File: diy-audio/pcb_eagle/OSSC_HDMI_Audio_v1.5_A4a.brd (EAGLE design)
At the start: 29.9 x 16.9 mm, 29 parts, among them U1 PCM1808, U2 74LVC1G34, U3 MK2507SLF

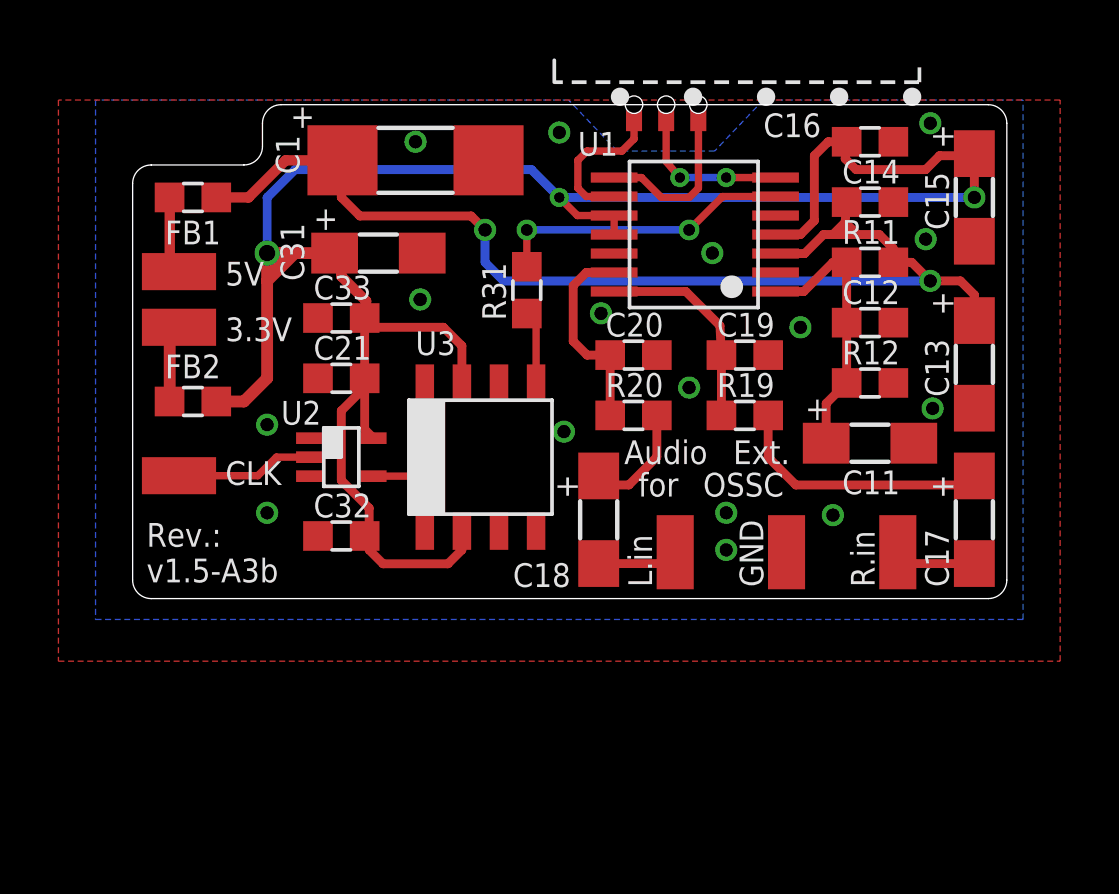
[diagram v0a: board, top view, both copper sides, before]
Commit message: PCB files with a pad for mclk to IT6613E
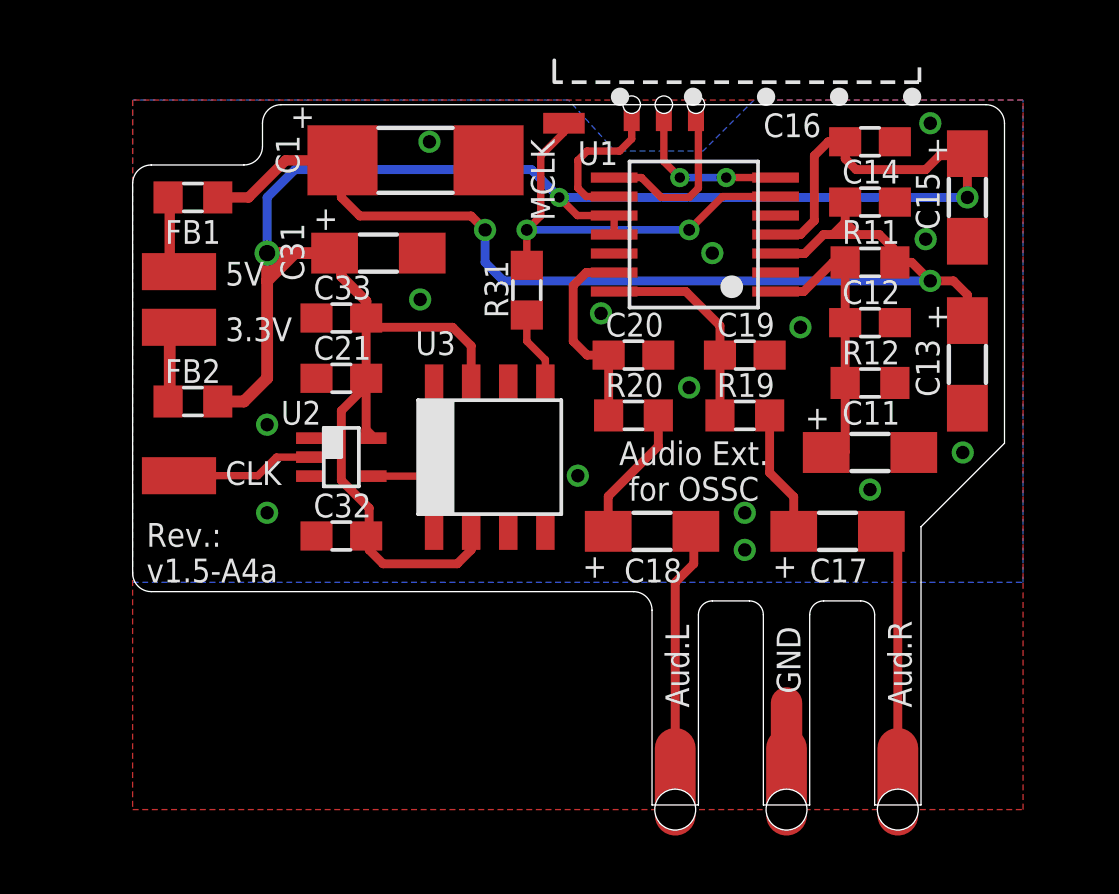
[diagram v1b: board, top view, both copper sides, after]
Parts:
- moved C17 4.70 mm to (24.1, 9.53), turned to 0 degrees
- moved C18 1.87 mm to (17.8, 9.53), turned to 0 degrees
- moved U3 0.32 mm to (12.2, 12.1)
- moved C11 0.32 mm to (25.2, 12.2)
- moved C13 0.24 mm to (28.6, 15.2)
- moved C15 0.24 mm to (28.6, 21.0)
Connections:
- net N$17: now also U$1.5
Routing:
- net N$1: track 2.76 -> 9.04 mm
- net N$2: track 2.76 -> 8.81 mm
- net N$3: track 9.03 -> 4.31 mm
- net N$17: track 10.3 -> 14.4 mm
- net GND: track 0.00 -> 3.65 mm, vias 16 -> 15
- net N$6: track 3.95 -> 4.68 mm
- net VCC/2: track 9.33 -> 9.94 mm
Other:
- board size 29.9 x 16.9 mm -> 29.8 x 24 mm
- board text added: "Aud.L"
- board text added: "Aud.R"
- board text added: "Audio Ext. for OSSC"
- board text added: "MCLK"
- board text added: "Rev.: v1.5-A4a"
- board text removed: "Audio"
- board text removed: "Ext."
- board text removed: "L.in"
- board text removed: "OSSC"
- board text removed: "R.in"
- board text removed: "Rev.: v1.5-A3b"
- board text removed: "for"
